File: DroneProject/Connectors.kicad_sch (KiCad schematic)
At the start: 8 parts, among them J21 Battery, J22 Debug, J23 UART, Q21 IRLML5203

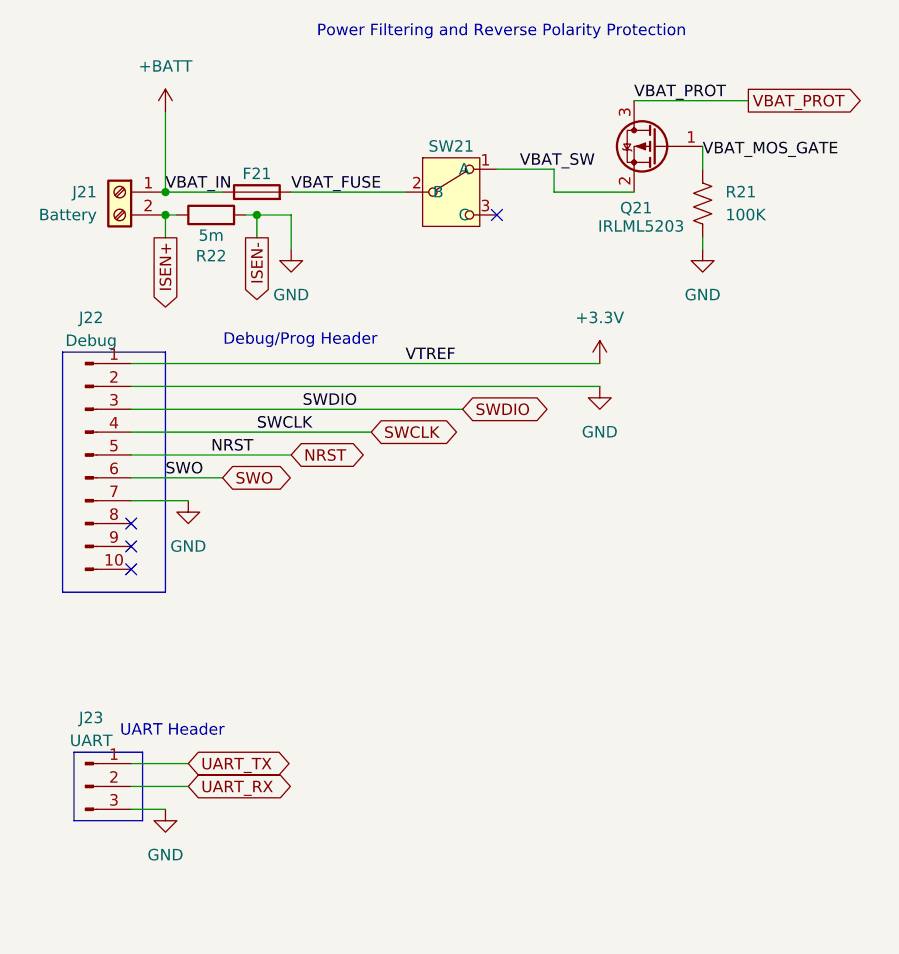
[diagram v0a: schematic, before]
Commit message: Added mounting holes and some more testpoints.  Also started on PCB with dimesions and mounting holes measured and placed
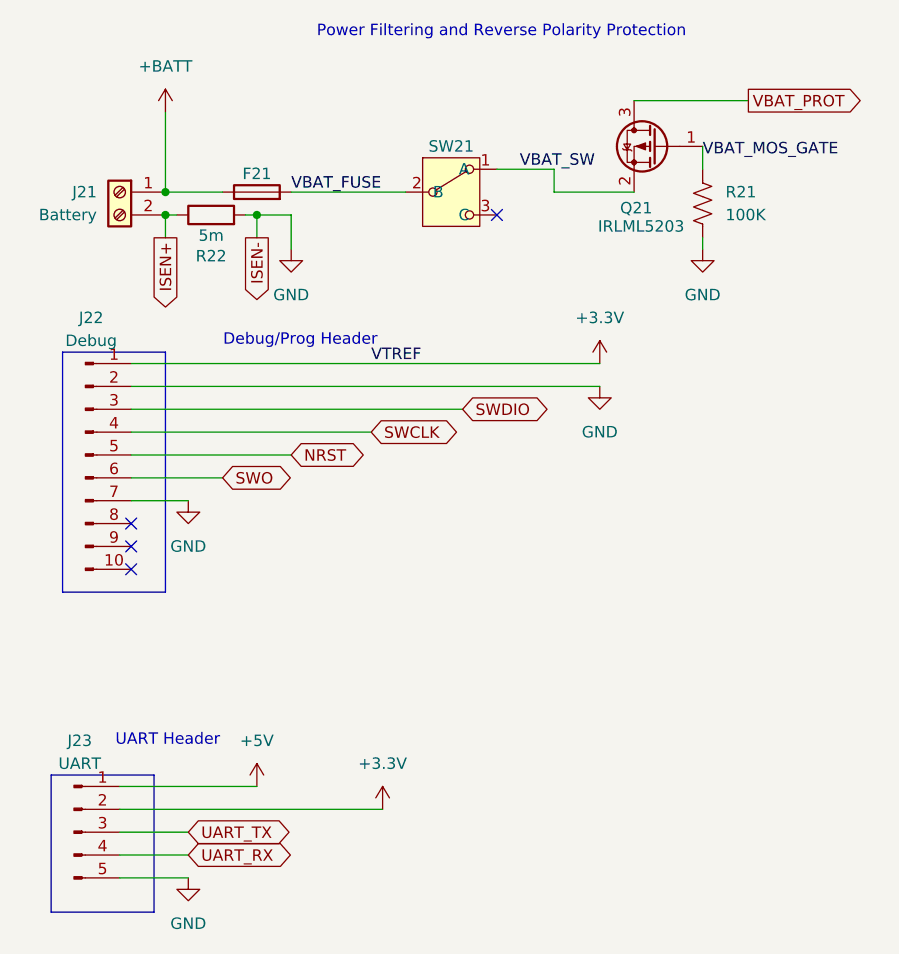
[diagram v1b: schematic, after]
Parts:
- removed J23: UART, symbol Connector:Conn_01x03_Pin
- added J23: UART, Connector_PinHeader_2.54mm:PinHeader_1x05_P2.54mm_Vertical, symbol Connector:Conn_01x05_Pin
- J21: footprint (none) -> Library:CUI_TB002-500-02BE
- J22: footprint (none) -> Connector_PinHeader_2.54mm:PinHeader_2x05_P2.54mm_Vertical
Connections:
- net +3.3V: now also J23.2 (Pin_2)
- net GND: now also J23.5 (Pin_5)
- net UART_RX: now also J23.4 (Pin_4)
- net UART_TX: now also J23.3 (Pin_3)
- new net +5V: J23.1 (Pin_1)

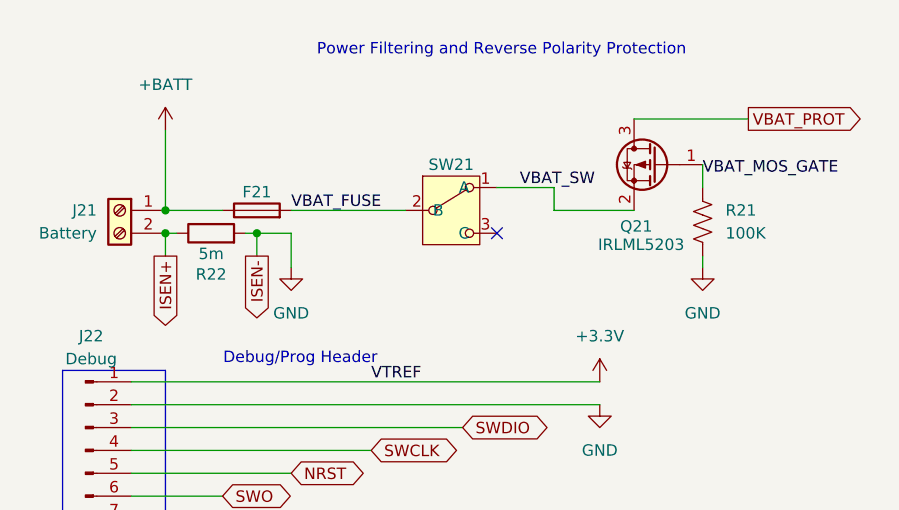
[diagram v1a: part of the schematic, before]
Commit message: Finished initial PCB layout.  However decided to go ahead and add the motor drivers for the first prototype anyways.  Re-did the reverse-polarity detection to use an NMOS instead of a PMOS.  Added sheets for each motor, still need to decide on parts.
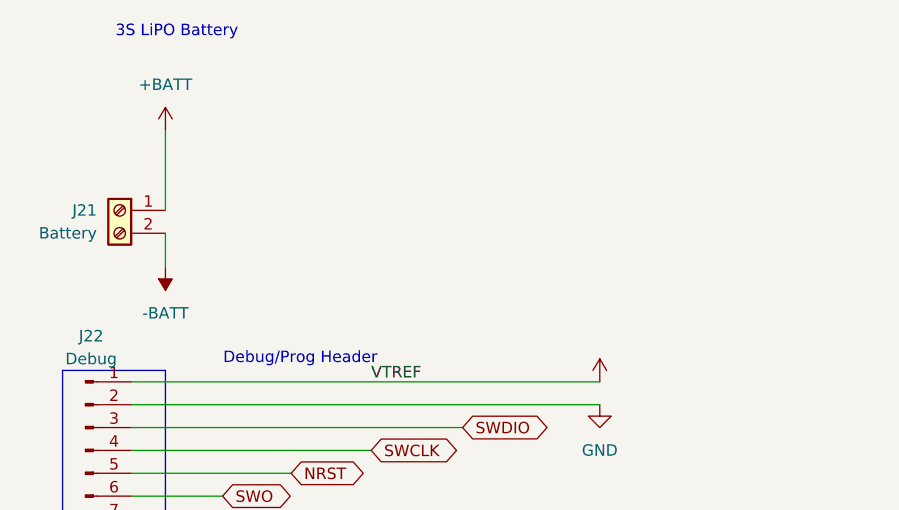
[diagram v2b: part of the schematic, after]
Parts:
- removed F21: Fuse, Fuse:Fuse_2920_7451Metric, symbol Device:Fuse
- removed Q21: IRLML5203, Package_TO_SOT_SMD:SOT-23, symbol Transistor_FET:IRLML5203
- removed R21: 100K, Resistor_SMD:R_0402_1005Metric, symbol Device:R_US
- removed R22: 5m, Resistor_SMD:R_2010_5025Metric, symbol Device:R
- removed SW21: ~, Library:SW_EG1218, symbol Global:EG1903-ND
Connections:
- net ISEN+ renamed -BATT
- no-connect marks 4 -> 3
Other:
- note added: "3S LiPO Battery"
- note removed: "Power Filtering and Reverse Polarity Protection"

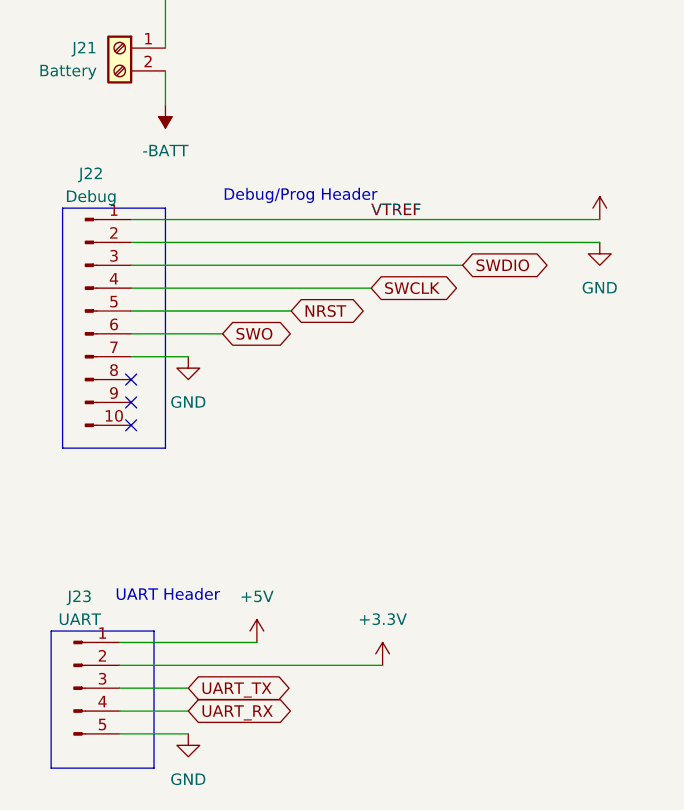
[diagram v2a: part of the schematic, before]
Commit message: Added a second MCU for motor control.  Removed 5V rail.  Added COM switching for SWD and UART external headers
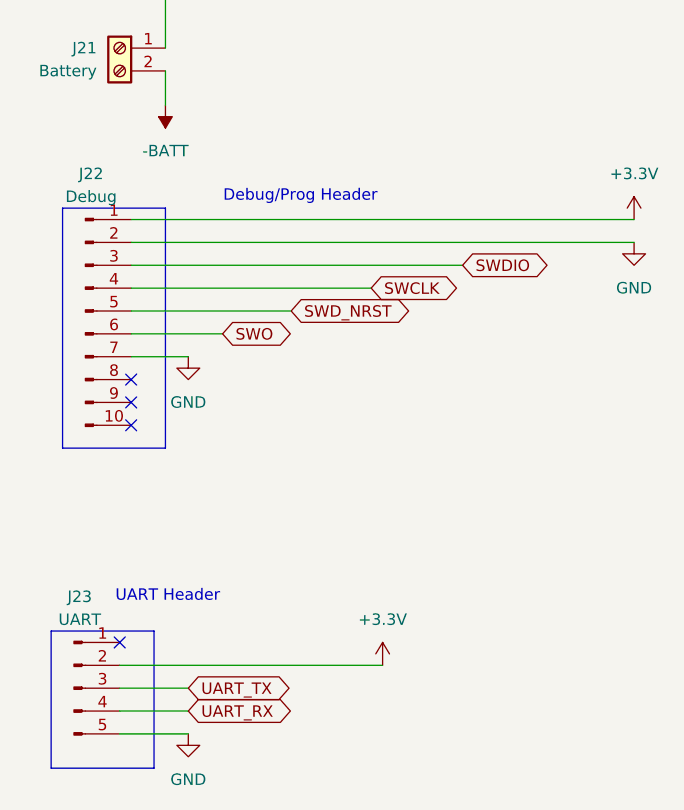
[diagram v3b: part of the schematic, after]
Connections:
- net +5V: no longer names the net of J23.1 (Pin_1)
- net NRST renamed SWD_NRST
- no-connect marks 3 -> 4
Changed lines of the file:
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@@
+	)
+	(no_connect
+		(at 40.64 127)
 	)
 	(no_connect
@@
 	(wire
 		(pts
-			(xy 41.91 82.55) (xy 93.98 82.55)
+			(xy 41.91 82.55) (xy 97.79 82.55)
 		)
 		(stroke
@@
 	(wire
 		(pts
-			(xy 41.91 80.01) (xy 93.98 80.01)
+			(xy 41.91 80.01) (xy 97.79 80.01)
 		)
 		(stroke
@@
 	(wire
 		(pts
-			(xy 40.64 127) (xy 55.88 127)
-		)
-		(stroke
-			(width 0)
-			(type default)
-		)
-	)
-	(wire
-		(pts
 			(xy 41.91 85.09) (xy 78.74 85.09)
 		)
@@
 		)
 	)
-	(label "VTREF"
-		(at 68.58 80.01 0)
+	(global_label "SWD_NRST"
+		(shape bidirectional)
+		(at 59.69 90.17 0)
+		(fields_autoplaced yes)
 		(effects
 			(font
 				(size 1.27 1.27)
 			)
-			(justify left bottom)
+			(justify left)
+		)
+		(property "Intersheetrefs" "${INTERSHEET_REFS}"
+			(at 73.4626 90.17 0)
+			(effects
+				(font
+					(size 1.27 1.27)
+				)
+				(justify left)
+			)
+		)
+	)
+	(global_label "SWCLK"
+		(shape bidirectional)
+		(at 68.58 87.63 0)
+		(fields_autoplaced yes)
+		(effects
+			(font
+				(size 1.27 1.27)
+			)
+			(justify left)
+		)
+		(property "Intersheetrefs" "${INTERSHEET_REFS}"
+			(at 78.9055 87.63 0)
+			(effects
+				(font
+					(size 1.27 1.27)
+				)
+				(justify left)
+			)
+		)
+	)
+	(global_label "UART_RX"
+		(shape bidirectional)
+		(at 48.26 134.62 0)
+		(fields_autoplaced yes)
+		(effects
+			(font
+				(size 1.27 1.27)
+			)
+			(justify left)
+		)
+		(property "Intersheetrefs" "${INTERSHEET_REFS}"
+			(at 60.4603 134.62 0)
+			(effects
+				(font
+					(size 1.27 1.27)
+				)
+				(justify left)
+			)
 		)
 	)
@@
 		)
 	)
-	(global_label "UART_RX"
+	(global_label "UART_TX"
 		(shape bidirectional)
-		(at 48.26 134.62 0)
+		(at 48.26 132.08 0)
 		(fields_autoplaced yes)
 		(effects
@@
 		)
 		(property "Intersheetrefs" "${INTERSHEET_REFS}"
-			(at 60.4603 134.62 0)
+			(at 60.1579 132.08 0)
 			(effects
 				(font
@@
 		)
 	)
-	(global_label "SWCLK"
+	(global_label "SWO"
 		(shape bidirectional)
-		(at 68.58 87.63 0)
+		(at 52.07 92.71 0)
 		(fields_autoplaced yes)
 		(effects
@@
 		)
 		(property "Intersheetrefs" "${INTERSHEET_REFS}"
-			(at 78.9055 87.63 0)
-			(effects
-				(font
-					(size 1.27 1.27)
-				)
-				(justify left)
-			)
-		)
-	)
-	(global_label "SWO"
-		(shape bidirectional)
-		(at 52.07 92.71 0)
-		(fields_autoplaced yes)
-		(effects
-			(font
-				(size 1.27 1.27)
-			)
-			(justify left)
-		)
-		(property "Intersheetrefs" "${INTERSHEET_REFS}"
 			(at 60.1579 92.71 0)
-			(effects
-				(font
-					(size 1.27 1.27)
-				)
-				(justify left)
-			)
-		)
-	)
-	(global_label "UART_TX"
-		(shape bidirectional)
-		(at 48.26 132.08 0)
-		(fields_autoplaced yes)
-		(effects
-			(font
-				(size 1.27 1.27)
-			)
-			(justify left)
-		)
-		(property "Intersheetrefs" "${INTERSHEET_REFS}"
-			(at 60.1579 132.08 0)
-			(effects
-				(font
-					(size 1.27 1.27)
-				)
-				(justify left)
-			)
-		)
-	)
-	(global_label "NRST"
-		(shape bidirectional)
-		(at 59.69 90.17 0)
-		(fields_autoplaced yes)
-		(effects
-			(font
-				(size 1.27 1.27)
-			)
-			(justify left)
-		)
-		(property "Intersheetrefs" "${INTERSHEET_REFS}"
-			(at 68.5641 90.17 0)
 			(effects
 				(font
@@
 	(symbol
 		(lib_id "power:+3.3V")
-		(at 93.98 80.01 0)
-		(unit 1)
-		(exclude_from_sim no)
-		(in_bom yes)
-		(on_board yes)
-		(dnp no)
-		(fields_autoplaced yes)
-		(property "Reference" "#PWR03"
-			(at 93.98 83.82 0)
-			(effects
-				(font
-					(size 1.27 1.27)
-				)
-				(hide yes)
-			)
-		)
-		(property "Value" "+3.3V"
-			(at 93.98 74.93 0)
-			(effects
-				(font
-					(size 1.27 1.27)
-				)
-				(hide yes)
-			)
-		)
-		(property "Footprint" ""
-			(at 93.98 80.01 0)
-			(effects
-				(font
-					(size 1.27 1.27)
-				)
-				(hide yes)
-			)
-		)
-		(property "Datasheet" ""
-			(at 93.98 80.01 0)
-			(effects
-				(font
-					(size 1.27 1.27)
-				)
-				(hide yes)
-			)
-		)
-		(property "Description" "Power symbol creates a global label with name \"+3.3V\""
-			(at 93.98 80.01 0)
-			(effects
-				(font
-					(size 1.27 1.27)
-				)
-				(hide yes)
-			)
-		)
-		(pin "1"
-		)
-		(instances
-			(project ""
-				(path "/feb4ca7b-5376-4689-a73b-f56020a5aa30/fd3a0c8b-dc0c-431b-b7b8-54b689ddfb8a"
-					(reference "#PWR03")
-					(unit 1)
-				)
-			)
-		)
-	)
-	(symbol
-		(lib_id "power:+3.3V")
 		(at 69.85 129.54 0)
 		(unit 1)
@@
 	)
 	(symbol
-		(lib_id "power:+5V")
-		(at 55.88 127 0)
-		(unit 1)
-		(exclude_from_sim no)
-		(in_bom yes)
-		(on_board yes)
-		(dnp no)
-		(fields_autoplaced yes)
-		(property "Reference" "#PWR088"
-			(at 55.88 130.81 0)
-			(effects
-				(font
-					(size 1.27 1.27)
-				)
-				(hide yes)
-			)
-		)
-		(property "Value" "+5V"
-			(at 55.88 121.92 0)
+		(lib_id "power:+3.3V")
+		(at 97.79 80.01 0)
+		(unit 1)
+		(exclude_from_sim no)
+		(in_bom yes)
+		(on_board yes)
+		(dnp no)
+		(fields_autoplaced yes)
+		(property "Reference" "#PWR03"
+			(at 97.79 83.82 0)
+			(effects
+				(font
+					(size 1.27 1.27)
+				)
+				(hide yes)
+			)
+		)
+		(property "Value" "+3.3V"
+			(at 97.79 74.93 0)
 			(effects
 				(font
@@
 		)
 		(property "Footprint" ""
-			(at 55.88 127 0)
+			(at 97.79 80.01 0)
 			(effects
 				(font
@@
 		)
 		(property "Datasheet" ""
-			(at 55.88 127 0)
-			(effects
-				(font
-					(size 1.27 1.27)
-				)
-				(hide yes)
-			)
-		)
-		(property "Description" "Power symbol creates a global label with name \"+5V\""
-			(at 55.88 127 0)
+			(at 97.79 80.01 0)
+			(effects
+				(font
+					(size 1.27 1.27)
+				)
+				(hide yes)
+			)
+		)
+		(property "Description" "Power symbol creates a global label with name \"+3.3V\""
+			(at 97.79 80.01 0)
 			(effects
 				(font
@@
 		)
 		(instances
-			(project ""
+			(project "DroneProject"
 				(path "/feb4ca7b-5376-4689-a73b-f56020a5aa30/fd3a0c8b-dc0c-431b-b7b8-54b689ddfb8a"
-					(reference "#PWR088")
+					(reference "#PWR03")
 					(unit 1)
 				)
@@
 	(symbol
 		(lib_id "power:GND")
-		(at 93.98 82.55 0)
+		(at 97.79 82.55 0)
 		(unit 1)
 		(exclude_from_sim no)
@@
 		(fields_autoplaced yes)
 		(property "Reference" "#PWR01"
-			(at 93.98 88.9 0)
+			(at 97.79 88.9 0)
 			(effects
 				(font
@@
 		)
 		(property "Value" "GND"
-			(at 93.98 87.63 0)
+			(at 97.79 87.63 0)
 			(effects
 				(font
@@
 		)
 		(property "Footprint" ""
-			(at 93.98 82.55 0)
+			(at 97.79 82.55 0)
 			(effects
 				(font
@@
 		)
 		(property "Datasheet" ""
-			(at 93.98 82.55 0)
+			(at 97.79 82.55 0)
 			(effects
 				(font
@@
 		)
 		(property "Description" "Power symbol creates a global label with name \"GND\" , ground"
-			(at 93.98 82.55 0)
-			(effects
-				(font
+			(at 97.79 82.55 0)
+			(effects
+				(font

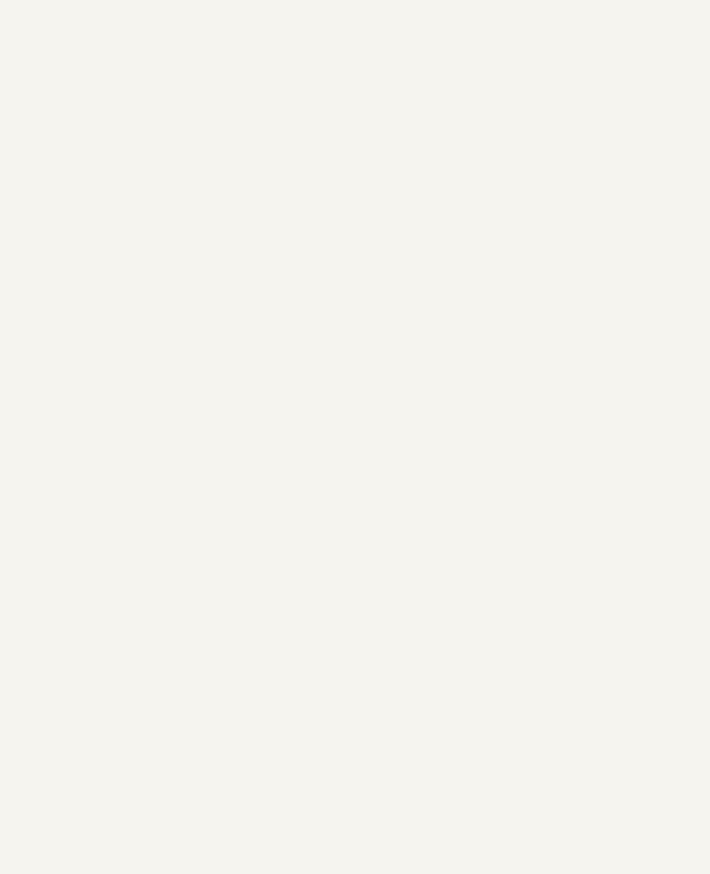
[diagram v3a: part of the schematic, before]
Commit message: Finished motor and C1 designs, still need to rename components on MTR2, 3, and 4 pages
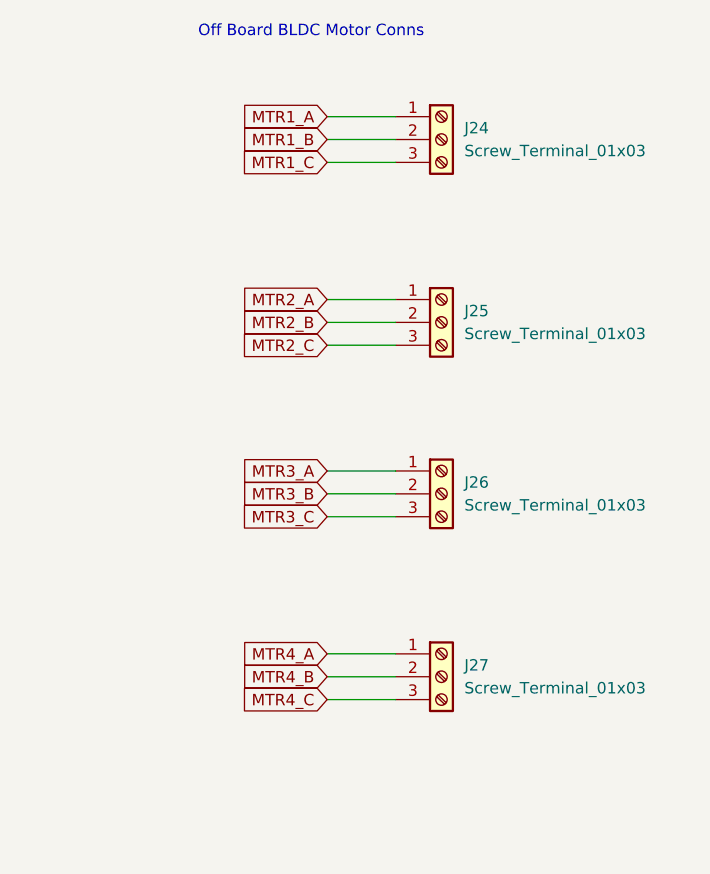
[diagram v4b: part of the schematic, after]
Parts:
- added J24, J25, J26, J27: Screw_Terminal_01x03, Library:CUI_TB005_-762-03BE, symbol Connector:Screw_Terminal_01x03
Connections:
- new net MTR1_A: J24.1 (Pin_1)
- new net MTR1_B: J24.2 (Pin_2)
- new net MTR1_C: J24.3 (Pin_3)
- new net MTR2_A: J25.1 (Pin_1)
- new net MTR2_B: J25.2 (Pin_2)
- new net MTR2_C: J25.3 (Pin_3)
- new net MTR3_A: J26.1 (Pin_1)
- new net MTR3_B: J26.2 (Pin_2)
- new net MTR3_C: J26.3 (Pin_3)
- new net MTR4_A: J27.1 (Pin_1)
- new net MTR4_B: J27.2 (Pin_2)
- new net MTR4_C: J27.3 (Pin_3)
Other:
- note added: "Off Board BLDC Motor Conns"

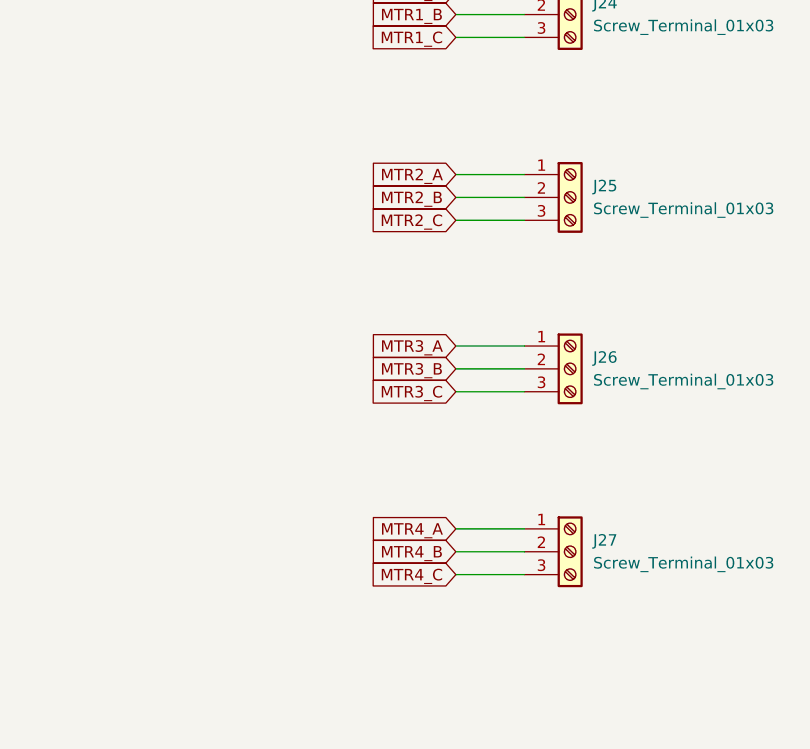
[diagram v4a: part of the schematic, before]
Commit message: Finished most of routing for motor controls, however likely going to revert back and make separate ESC boards for motor control as I think that would honestly be more efficient from both a cost and debug complexity standpoint.
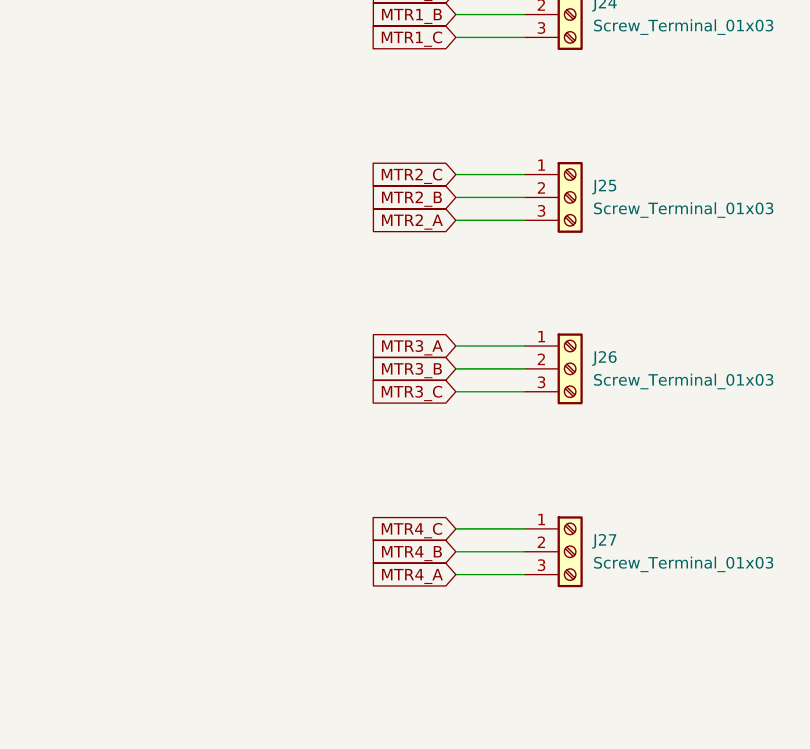
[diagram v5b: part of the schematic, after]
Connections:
- net MTR2_A: now also J25.3 (Pin_3); no longer J25.1 (Pin_1)
- net MTR2_C: now also J25.1 (Pin_1); no longer J25.3 (Pin_3)
- net MTR4_A: now also J27.3 (Pin_3); no longer J27.1 (Pin_1)
- net MTR4_C: now also J27.1 (Pin_1); no longer J27.3 (Pin_3)
